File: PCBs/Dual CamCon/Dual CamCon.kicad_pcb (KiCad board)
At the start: 2 copper layers, 56 x 65 mm, 14 parts, among them J1 Servo In, J2 Servo In, J3 Camera In, J4 Camera In, J5 Raspberry Pi GPIO, P1 HDMI Out, P2 HDMI Out

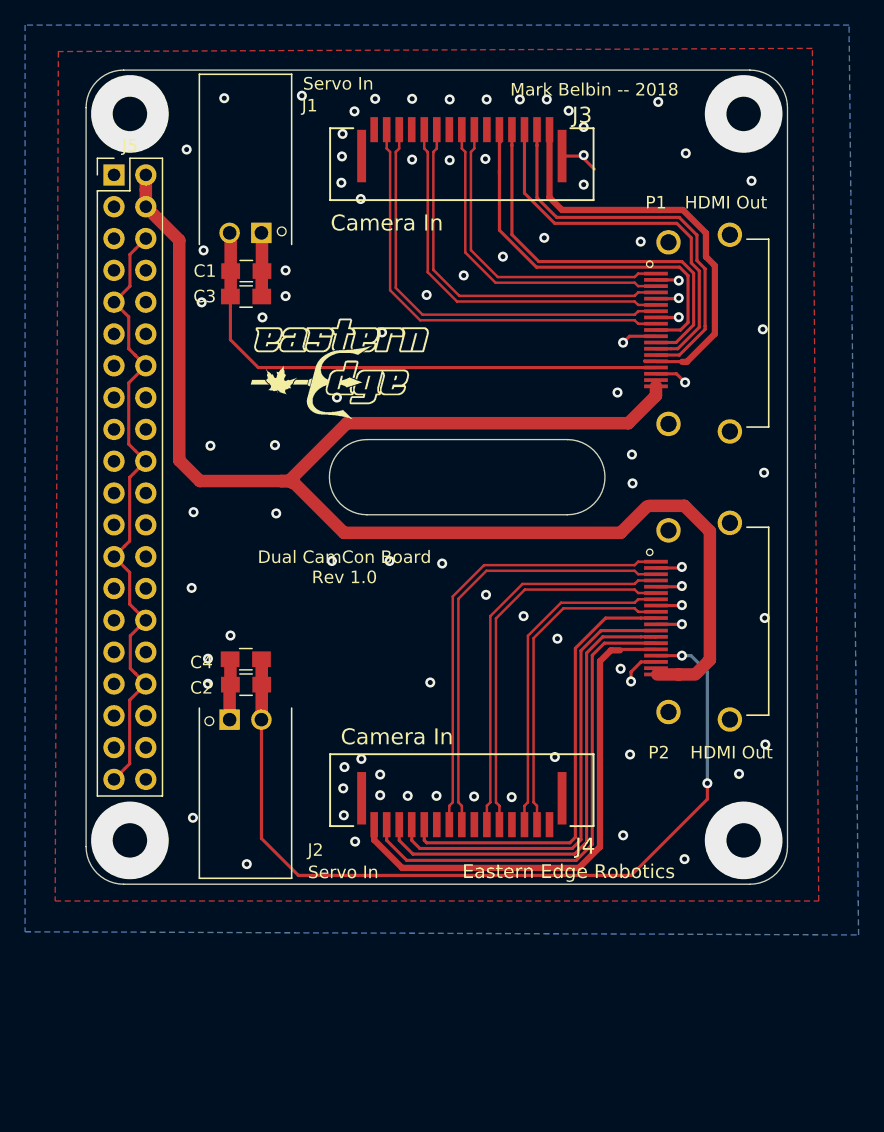
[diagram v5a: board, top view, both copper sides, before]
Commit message: Started DC-DC with Micro
Picked out microcontroller maybe? Still gotta decide if I want to use the 5x5 vs the 7x7.
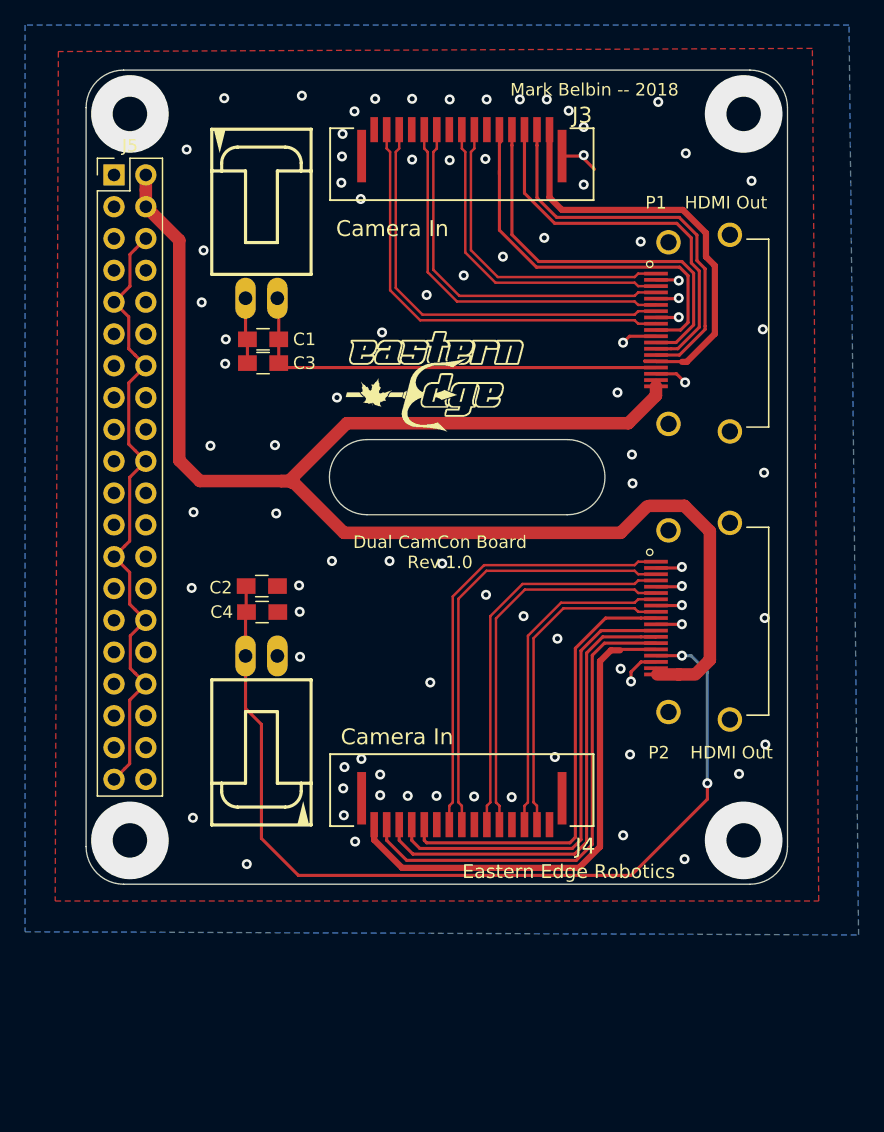
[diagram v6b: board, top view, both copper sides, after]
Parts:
- J1, J2: value Servo In -> Servo Input; footprint EER:MOLEX_0705530001 -> EER:70553-02
- J5: footprint EER:RaspberryGPIO -> Pin_Headers:Pin_Header_Straight_2x20_Pitch2.54mm
- P1, P2: footprint FCI_10029449-001RLF -> EER:FCI_10029449-001RLF
- moved C2 7.97 mm to (114.0, 76.2), turned to 0 degrees
- moved ? 7.64 mm to (118.2, 65.6)
- moved C1 5.61 mm to (114.1, 56.5), turned to 180 degrees
- moved C3 5.49 mm to (114.1, 58.4), turned to 180 degrees
- moved C4 3.98 mm to (114.1, 78.3), turned to 0 degrees
- moved J2 3.59 mm to (114.0, 89.4), turned to 180 degrees
- moved J1 2.40 mm to (114.0, 45.6), turned to 0 degrees
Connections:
- P1 pad P1: GND -> (no net)
- P1 pad P2: GND -> (no net)
- P1 pad P3: GND -> (no net)
- P1 pad P4: GND -> (no net)
- P2 pad P1: GND -> (no net)
- P2 pad P2: GND -> (no net)
- P2 pad P3: GND -> (no net)
- P2 pad P4: GND -> (no net)
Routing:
- net /Servo1: track 43.5 -> 35.6 mm
- net /Servo2: track 68.6 -> 74.9 mm
- net GND: track 86.8 -> 82.0 mm, vias 87 -> 86

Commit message: Small Tweaks
3D Model for RPi GPIO on the CamCon was wrong.
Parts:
- J5: footprint Pin_Headers:Pin_Header_Straight_2x20_Pitch2.54mm -> EER:RaspberryGPIO

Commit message: CamCon and BOM Stuff
Working hard on the bomssss.
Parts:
- moved J5 48.3 mm to (104.8, 91.6), turned to 180 degrees
- moved C1 4.91 mm to (114.3, 61.4)
- moved C3 4.91 mm to (114.3, 63.3)
- moved J1 4.91 mm to (114.1, 50.5)
- moved C4 4.09 mm to (114.2, 74.2)
- moved J2 4.09 mm to (114.2, 85.3)
- moved C2 4.09 mm to (114.2, 72.1)
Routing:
- net GND: track 82.0 -> 31.4 mm
- net /Servo2: track 74.9 -> 78.9 mm
- net +5V: track 122.4 -> 123.1 mm
- added copper zone on F.Cu, net +5V
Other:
- net class 5V added: clearance 0.2, trace_width 1, via_dia 0.8, via_drill 0.4
- board text added: "Dual CamCon Board Rev 1.1"
- board text removed: "Dual CamCon Board Rev 1.0"
